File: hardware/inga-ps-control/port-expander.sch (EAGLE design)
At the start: 6 parts, among them IC1 PCF8574P, IC2 PCF8574P

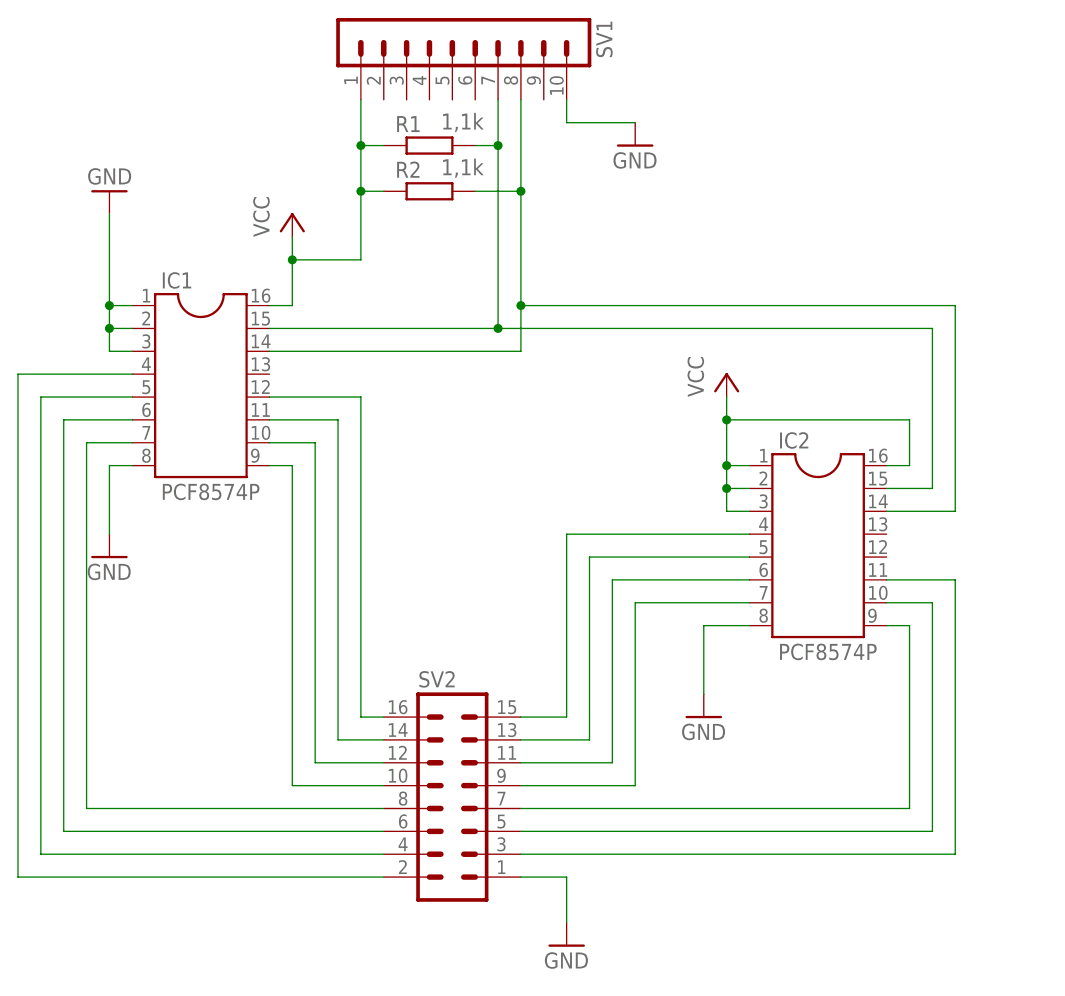
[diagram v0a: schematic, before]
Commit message: added labels
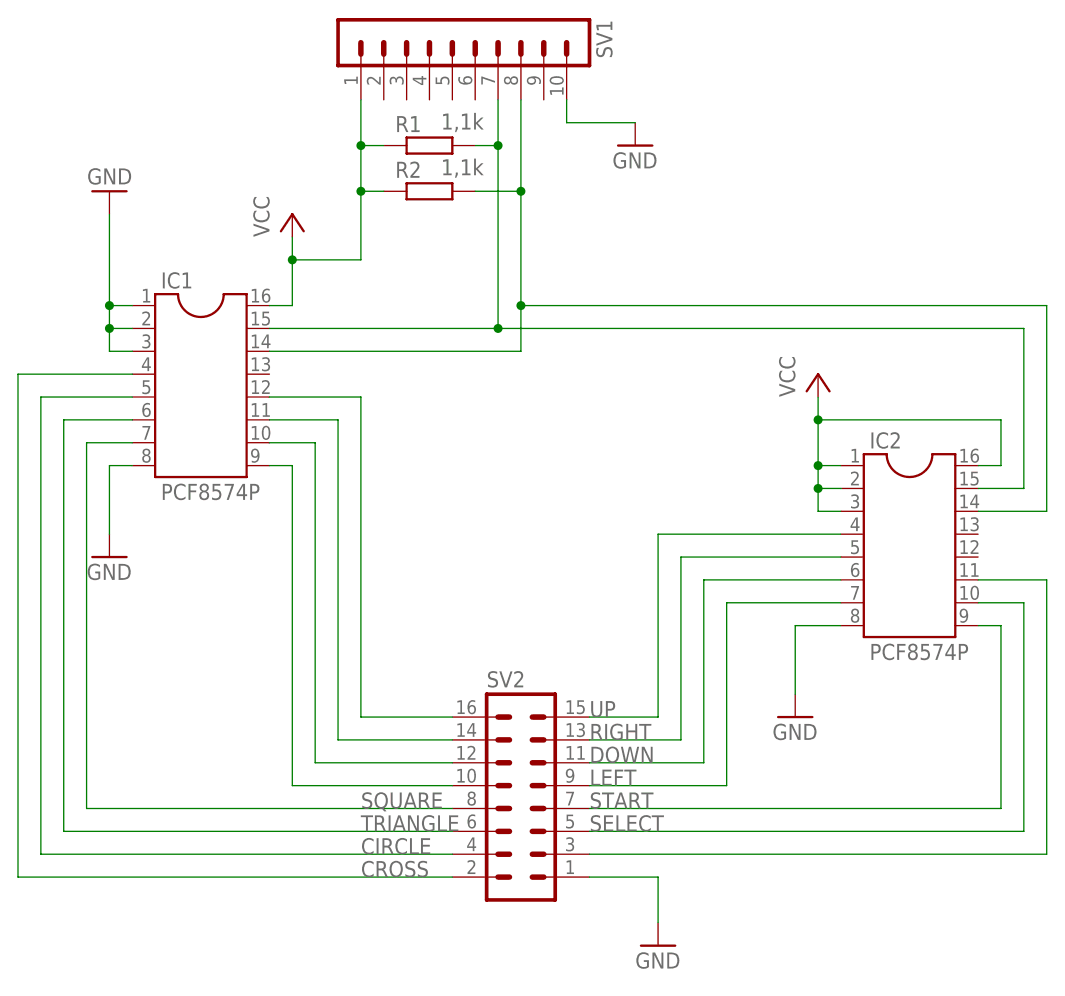
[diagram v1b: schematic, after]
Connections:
- net N$1 renamed UP
- net N$11 renamed DOWN
- net N$12 renamed LEFT
- net N$13 renamed START
- net N$14 renamed SELECT
- net N$2 renamed RIGHT
- net N$3 renamed CROSS
- net N$4 renamed CIRCLE
- net N$5 renamed TRIANGLE
- net N$6 renamed SQUARE
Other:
- moved on the sheet: IC2, SV2
